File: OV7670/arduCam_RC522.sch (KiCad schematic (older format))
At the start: 3 parts, among them J1 OV7670, J2 PMOD1, J3 PMOD2

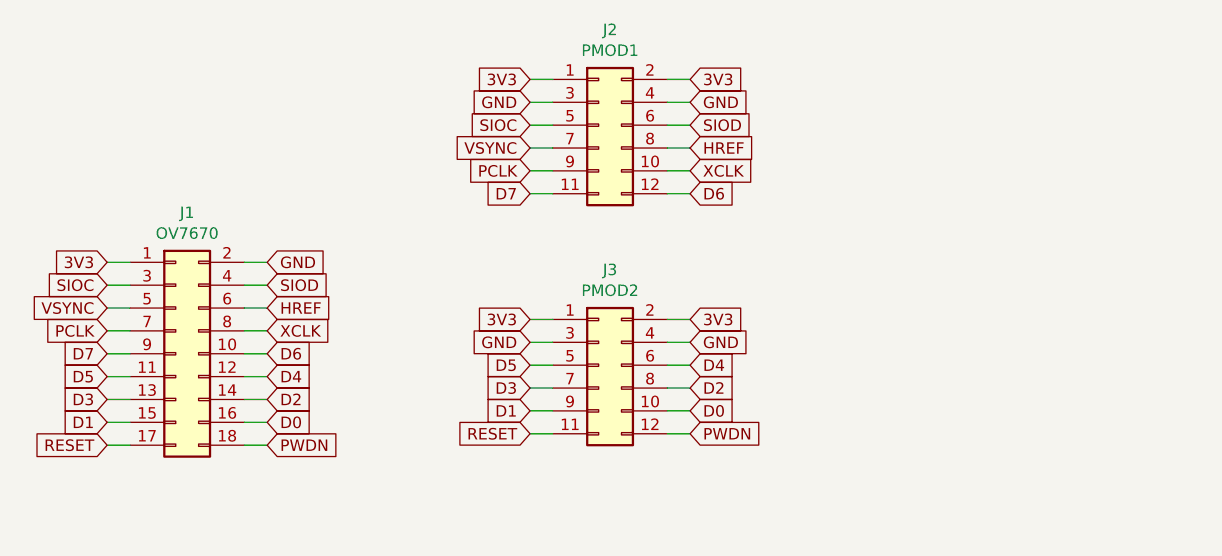
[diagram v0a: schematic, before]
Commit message: Adding pcb for camera
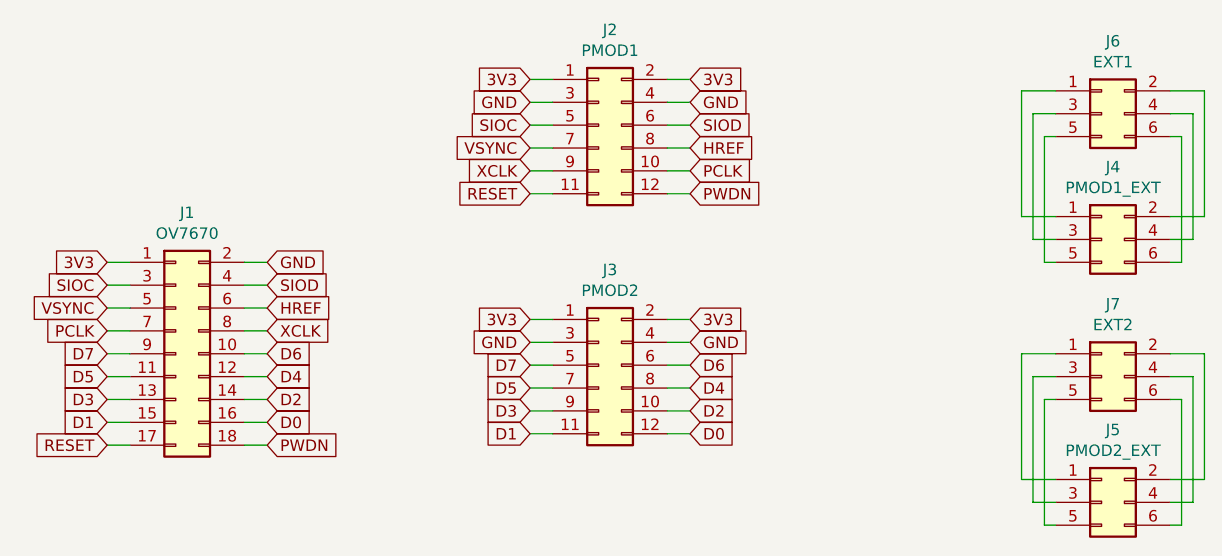
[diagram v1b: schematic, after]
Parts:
- added J4: PMOD1_EXT, Connector_PinHeader_2.54mm:PinHeader_2x03_P2.54mm_Horizontal, symbol Connector_Generic:Conn_02x03_Odd_Even
- added J5: PMOD2_EXT, Connector_PinHeader_2.54mm:PinHeader_2x03_P2.54mm_Horizontal, symbol Connector_Generic:Conn_02x03_Odd_Even
- added J6: EXT1, Connector_PinHeader_2.54mm:PinHeader_2x03_P2.54mm_Vertical, symbol Connector_Generic:Conn_02x03_Odd_Even
- added J7: EXT2, Connector_PinHeader_2.54mm:PinHeader_2x03_P2.54mm_Vertical, symbol Connector_Generic:Conn_02x03_Odd_Even
- J1: footprint (none) -> Connector_PinHeader_2.54mm:PinHeader_2x09_P2.54mm_Horizontal
- J2, J3: footprint (none) -> Connector_PinHeader_2.54mm:PinHeader_2x06_P2.54mm_Horizontal
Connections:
- net D0: now also J3.12 (Pin_12); no longer J3.10 (Pin_10)
- net D1: now also J3.11 (Pin_11); no longer J3.9 (Pin_9)
- net D2: now also J3.10 (Pin_10); no longer J3.8 (Pin_8)
- net D3: now also J3.9 (Pin_9); no longer J3.7 (Pin_7)
- net D4: now also J3.8 (Pin_8); no longer J3.6 (Pin_6)
- net D5: now also J3.7 (Pin_7); no longer J3.5 (Pin_5)
- net D6: now also J3.6 (Pin_6); no longer J2.12 (Pin_12)
- net D7: now also J3.5 (Pin_5); no longer J2.11 (Pin_11)
- net PCLK: now also J2.10 (Pin_10); no longer J2.9 (Pin_9)
- net PWDN: now also J2.12 (Pin_12); no longer J3.12 (Pin_12)
- net RESET: now also J2.11 (Pin_11); no longer J3.11 (Pin_11)
- net XCLK: now also J2.9 (Pin_9); no longer J2.10 (Pin_10)
- new net: J4.1 (Pin_1), J6.1 (Pin_1)
- new net: J4.2 (Pin_2), J6.2 (Pin_2)
- new net: J4.3 (Pin_3), J6.3 (Pin_3)
- new net: J4.4 (Pin_4), J6.4 (Pin_4)
- new net: J4.5 (Pin_5), J6.5 (Pin_5)
- new net: J4.6 (Pin_6), J6.6 (Pin_6)
- new net: J5.1 (Pin_1), J7.1 (Pin_1)
- new net: J5.2 (Pin_2), J7.2 (Pin_2)
- new net: J5.3 (Pin_3), J7.3 (Pin_3)
- new net: J5.4 (Pin_4), J7.4 (Pin_4)
- new net: J5.5 (Pin_5), J7.5 (Pin_5)
- new net: J5.6 (Pin_6), J7.6 (Pin_6)
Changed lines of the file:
@@
 EESchema Schematic File Version 4
+LIBS:arduCam_RC522-cache
 EELAYER 26 0
 EELAYER END
@@
 F 0 "J1" H 5750 4867 50  0000 C CNN
 F 1 "OV7670" H 5750 4776 50  0000 C CNN
-F 2 "" H 5700 4250 50  0001 C CNN
+F 2 "Connector_PinHeader_2.54mm:PinHeader_2x09_P2.54mm_Horizontal" H 5700 4250 50  0001 C CNN
 F 3 "~" H 5700 4250 50  0001 C CNN
 	1    5700 4250
@@
 F 0 "J2" H 7600 3667 50  0000 C CNN
 F 1 "PMOD1" H 7600 3576 50  0000 C CNN
-F 2 "" H 7550 3250 50  0001 C CNN
+F 2 "Connector_PinHeader_2.54mm:PinHeader_2x06_P2.54mm_Horizontal" H 7550 3250 50  0001 C CNN
 F 3 "~" H 7550 3250 50  0001 C CNN
 	1    7550 3250
@@
 Text GLabel 7950 3350 2    50   Input ~ 0
 HREF
+Text GLabel 7950 3450 2    50   Input ~ 0
+PCLK
 Text GLabel 7250 3450 0    50   Input ~ 0
-PCLK
-Text GLabel 7950 3450 2    50   Input ~ 0
 XCLK
+Text GLabel 7250 4300 0    50   Input ~ 0
+D7
+Text GLabel 7950 4300 2    50   Input ~ 0
+D6
+Text GLabel 7250 4400 0    50   Input ~ 0
+D5
+Text GLabel 7250 4500 0    50   Input ~ 0
+D3
+Text GLabel 7250 4600 0    50   Input ~ 0
+D1
 Text GLabel 7250 3550 0    50   Input ~ 0
-D7
-Text GLabel 7950 3550 2    50   Input ~ 0
-D6
-Text GLabel 7250 4300 0    50   Input ~ 0
-D5
-Text GLabel 7250 4400 0    50   Input ~ 0
-D3
-Text GLabel 7250 4500 0    50   Input ~ 0
-D1
-Text GLabel 7250 4600 0    50   Input ~ 0
 RESET
-Text GLabel 7950 4300 2    50   Input ~ 0
+Text GLabel 7950 4400 2    50   Input ~ 0
 D4
-Text GLabel 7950 4400 2    50   Input ~ 0
+Text GLabel 7950 4500 2    50   Input ~ 0
 D2
-Text GLabel 7950 4500 2    50   Input ~ 0
+Text GLabel 7950 4600 2    50   Input ~ 0
 D0
 Text GLabel 7950 4200 2    50   Input ~ 0
@@
 F 0 "J3" H 7600 4717 50  0000 C CNN
 F 1 "PMOD2" H 7600 4626 50  0000 C CNN
-F 2 "" H 7550 4300 50  0001 C CNN
+F 2 "Connector_PinHeader_2.54mm:PinHeader_2x06_P2.54mm_Horizontal" H 7550 4300 50  0001 C CNN
 F 3 "~" H 7550 4300 50  0001 C CNN
 	1    7550 4300
 	1    0    0    -1
 $EndComp
-Text GLabel 7950 4600 2    50   Input ~ 0
+Text GLabel 7950 3550 2    50   Input ~ 0
 PWDN
 Wire Wire Line
@@
 Wire Wire Line
 	7250 4600 7350 4600
+$Comp
+L Connector_Generic:Conn_02x03_Odd_Even J4
+U 1 1 5BFD989D
+P 9750 3750
+F 0 "J4" H 9800 4067 50  0000 C CNN
+F 1 "PMOD1_EXT" H 9800 3976 50  0000 C CNN
+F 2 "Connector_PinHeader_2.54mm:PinHeader_2x03_P2.54mm_Horizontal" H 9750 3750 50  0001 C CNN
+F 3 "~" H 9750 3750 50  0001 C CNN
+	1    9750 3750
+	1    0    0    -1
+$EndComp
+$Comp
+L Connector_Generic:Conn_02x03_Odd_Even J5
+U 1 1 5BFD99E9
+P 9750 4900
+F 0 "J5" H 9800 5217 50  0000 C CNN
+F 1 "PMOD2_EXT" H 9800 5126 50  0000 C CNN
+F 2 "Connector_PinHeader_2.54mm:PinHeader_2x03_P2.54mm_Horizontal" H 9750 4900 50  0001 C CNN
+F 3 "~" H 9750 4900 50  0001 C CNN
+	1    9750 4900
+	1    0    0    -1
+$EndComp
+$Comp
+L Connector_Generic:Conn_02x03_Odd_Even J6
+U 1 1 5BFD9AAC
+P 9750 3200
+F 0 "J6" H 9800 3517 50  0000 C CNN
+F 1 "EXT1" H 9800 3426 50  0000 C CNN
+F 2 "Connector_PinHeader_2.54mm:PinHeader_2x03_P2.54mm_Vertical" H 9750 3200 50  0001 C CNN
+F 3 "~" H 9750 3200 50  0001 C CNN
+	1    9750 3200
+	1    0    0    -1
+$EndComp
+$Comp
+L Connector_Generic:Conn_02x03_Odd_Even J7
+U 1 1 5BFD9AE4
+P 9750 4350
+F 0 "J7" H 9800 4667 50  0000 C CNN
+F 1 "EXT2" H 9800 4576 50  0000 C CNN
+F 2 "Connector_PinHeader_2.54mm:PinHeader_2x03_P2.54mm_Vertical" H 9750 4350 50  0001 C CNN
+F 3 "~" H 9750 4350 50  0001 C CNN
+	1    9750 4350
+	1    0    0    -1
+$EndComp
+Wire Wire Line
+	9550 4250 9400 4250
+Wire Wire Line
+	9400 4250 9400 4800
+Wire Wire Line
+	9400 4800 9550 4800
+Wire Wire Line
+	9550 4350 9450 4350
+Wire Wire Line
+	9450 4350 9450 4900
+Wire Wire Line
+	9450 4900 9550 4900
+Wire Wire Line
+	9550 4450 9500 4450
+Wire Wire Line
+	9500 4450 9500 5000
+Wire Wire Line
+	9500 5000 9550 5000
+Wire Wire Line
+	10050 4450 10100 4450
+Wire Wire Line
+	10100 4450 10100 5000
+Wire Wire Line
+	10100 5000 10050 5000
+Wire Wire Line
+	10050 4900 10150 4900
+Wire Wire Line
+	10150 4900 10150 4350
+Wire Wire Line
+	10150 4350 10050 4350
+Wire Wire Line
+	10050 4250 10200 4250
+Wire Wire Line
+	10200 4250 10200 4800
+Wire Wire Line
+	10200 4800 10050 4800
+Wire Wire Line
+	9550 3200 9450 3200
+Wire Wire Line
+	9450 3200 9450 3750
+Wire Wire Line
+	9450 3750 9550 3750
+Wire Wire Line
+	9550 3300 9500 3300
+Wire Wire Line
+	9500 3300 9500 3850
+Wire Wire Line
+	9500 3850 9550 3850
+Wire Wire Line
+	10050 3850 10100 3850
+Wire Wire Line
+	10100 3850 10100 3300
+Wire Wire Line
+	10100 3300 10050 3300
+Wire Wire Line
+	10050 3200 10150 3200
+Wire Wire Line
+	10150 3200 10150 3750
+Wire Wire Line
+	10150 3750 10050 3750
+Wire Wire Line
+	10050 3650 10200 3650
+Wire Wire Line
+	10200 3650 10200 3100
+Wire Wire Line
+	10200 3100 10050 3100
+Wire Wire Line
+	9550 3100 9400 3100
+Wire Wire Line
+	9400 3100 9400 3650
+Wire Wire Line
+	9400 3650 9550 3650
 $EndSCHEMATC
